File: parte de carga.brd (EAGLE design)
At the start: 74.6 x 102.9 mm, 33 parts, among them IC1 MCP73831T-2ACI_OT, IC10 741G3157DBVR, IC15 LMV321AIDCKR, IC16 LMV321AIDCKR, IC2 ESP32-S3-WROOM-1-N16R8, IC5 LMV321AIDCKR, IC7 AD8226ARZ, IC9 LP38692MP-3.3_NOPB, J1 USB3500-30-A-KIT

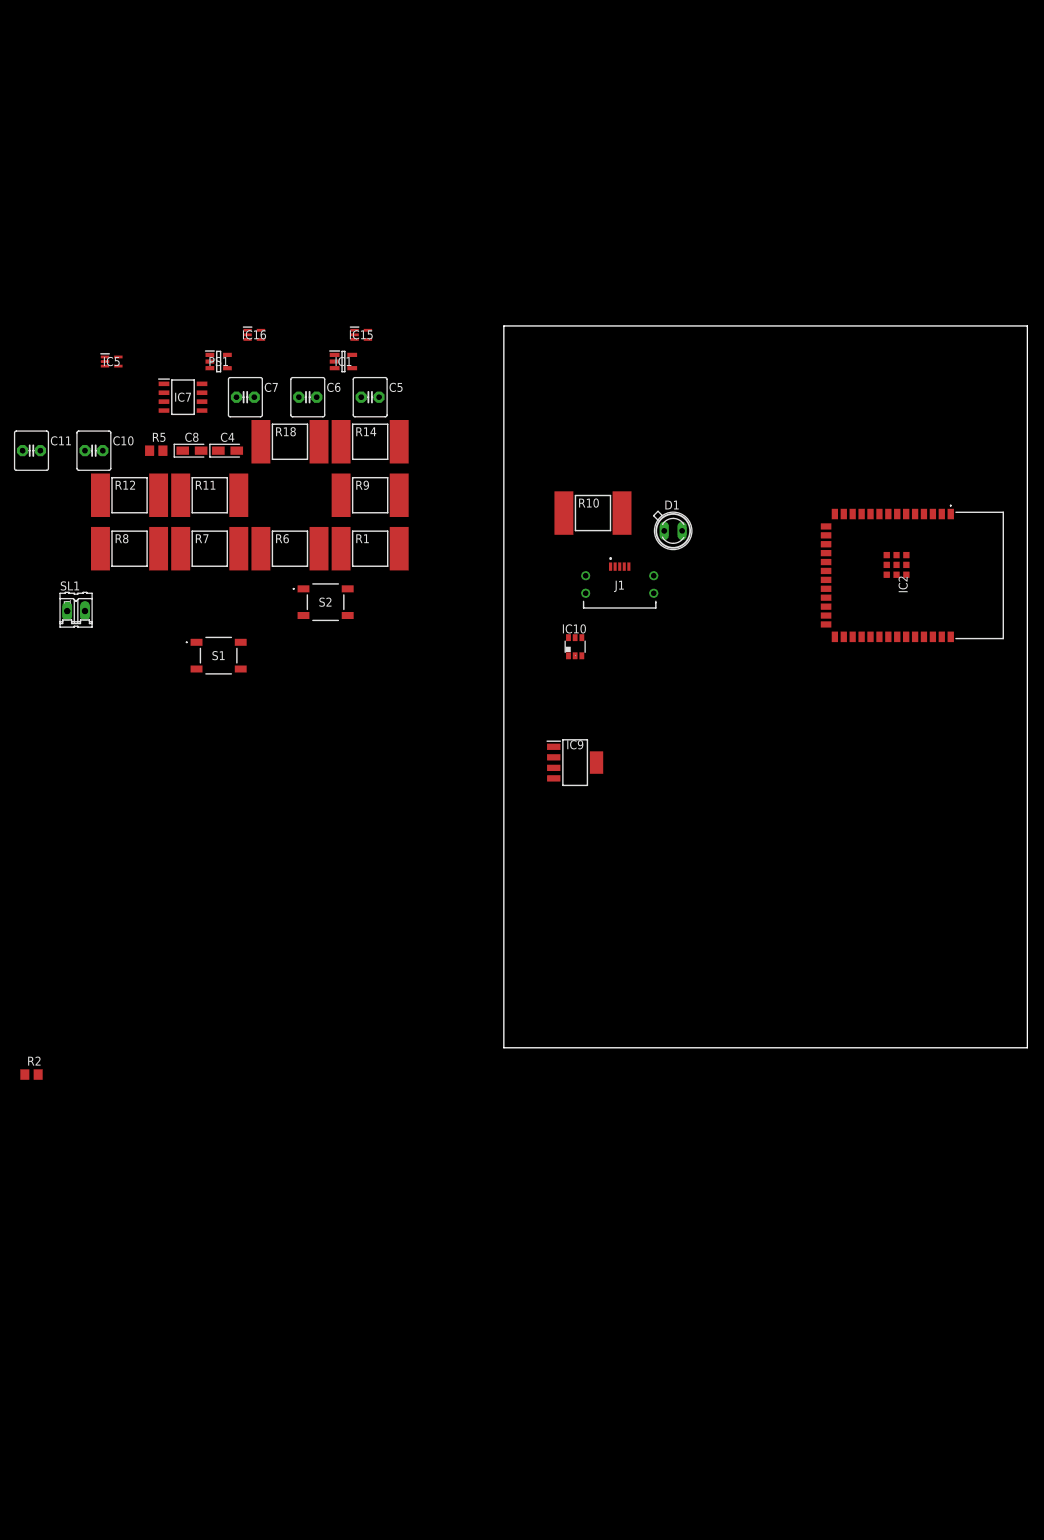
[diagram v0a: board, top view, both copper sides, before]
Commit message: arregle las resistencias, condensadores y diodo
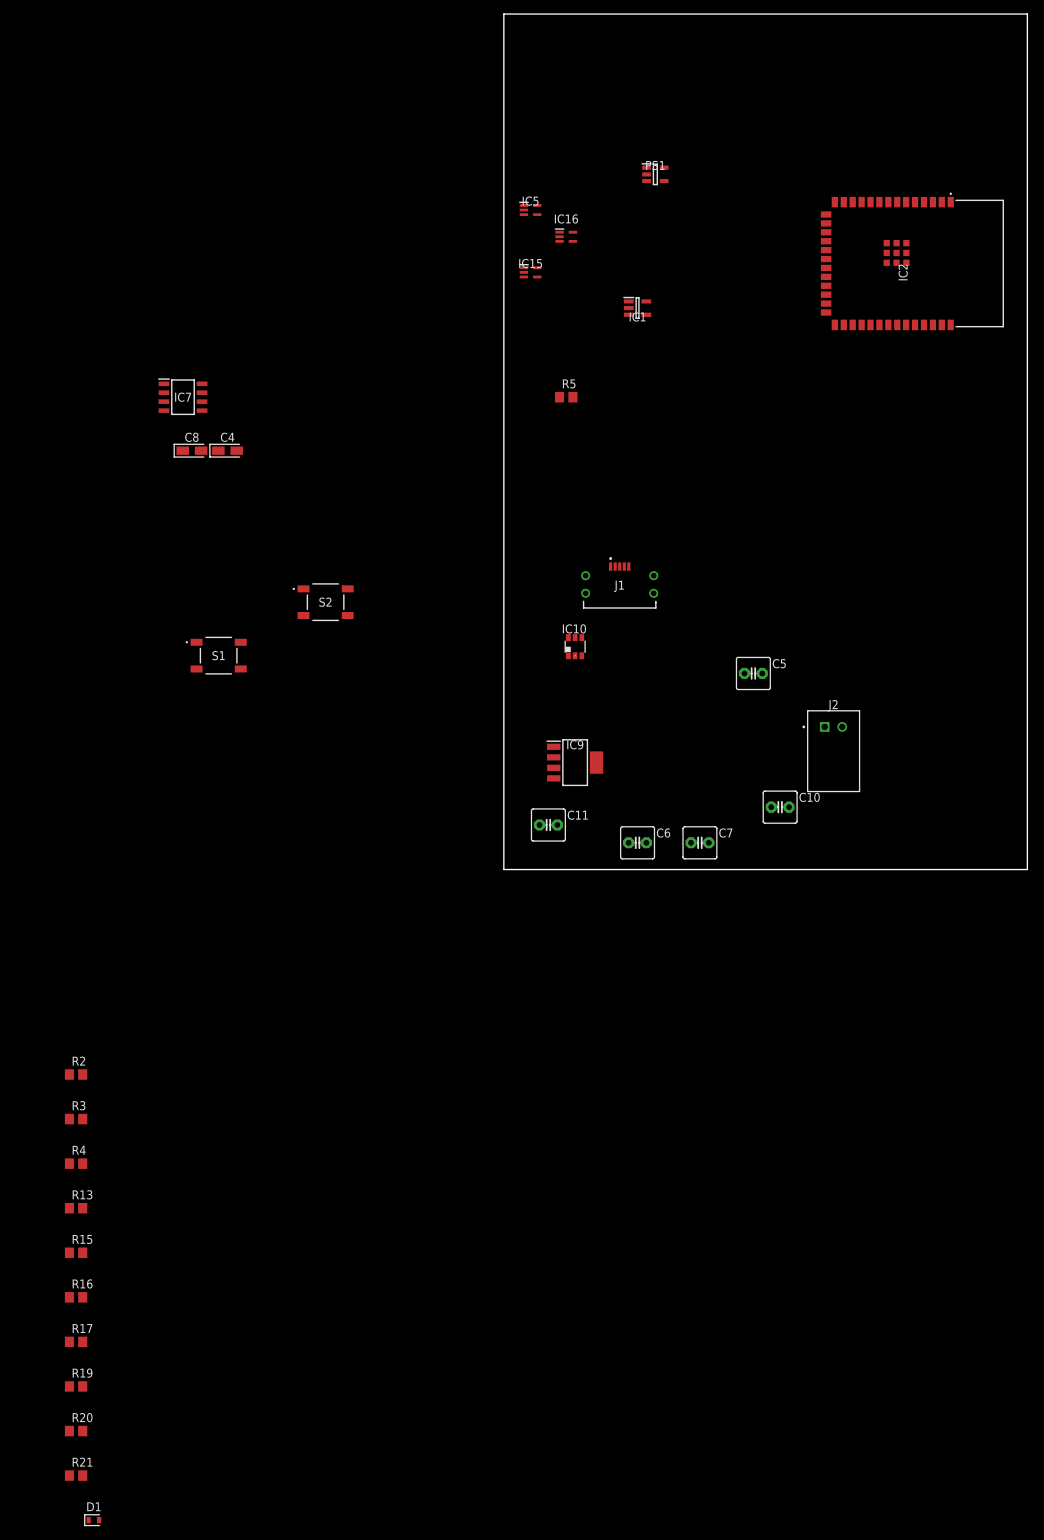
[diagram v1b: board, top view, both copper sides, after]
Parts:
- removed R1: 2k, resistor-shunt:BVS
- removed R10: 220, resistor-shunt:BVS
- removed R11, R12, R8: 10k, resistor-shunt:BVS
- removed R14: 1.6k, resistor-shunt:BVS
- removed R18, R9: 450, resistor-shunt:BVS
- removed R6: 3.2k, resistor-shunt:BVS
- removed R7: 1k, resistor-shunt:BVS
- removed SL1: (no value), con-amp-quick:02P
- added J2: S2B-XH-A, Connector:S2B-XH-A
- added R13: 1.6k, rcl:R0805
- added R15, R21, R4: 10k, rcl:R0805
- added R16: 3.2k, rcl:R0805
- added R17: 1k, rcl:R0805
- added R19, R20: 450, rcl:R0805
- added R3: 2k, rcl:R0805
- C10, C11, C5, C6, C7: device capacitor-wima:C2.5-6 -> capacitor-wima:C2.5-5
- D1: value SFH482 -> CHIP-FLAT-G_0603-0.35MM; device led:SFH482 -> LED:LEDC1608X35N_FLAT-G
- R2: value (none) -> 220
- moved D1 163.4 mm to (-58.4, -90.2)
- moved C10 110.2 mm to (39.4, 11.4)
- moved C11 90.9 mm to (6.35, 8.89)
- moved C7 90.7 mm to (27.9, 6.35)
- moved C6 79.0 mm to (19.1, 6.35)
- moved PS1 67.7 mm to (21.6, 101.6)
- moved C5 67.3 mm to (35.6, 30.5)
- moved IC5 63.5 mm to (3.81, 96.5)
- moved R5 58.9 mm to (8.89, 69.8)
- moved IC16 46.6 mm to (8.89, 92.7)
- moved IC2 44.5 mm to (58.4, 88.9)
- moved IC1 42.6 mm to (19.1, 82.5)
- moved IC15 25.7 mm to (3.81, 87.6)
- moved R2 6.35 mm to (-61.0, -26.7)
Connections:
- removed net N$7: C7.1, IC5.4, R9.1
- new net N$14: C5.2, R13.1
- net +5V: now also R21.2, R4.2; no longer R11.1, R12.1
- net +BATT: now also J2.1; no longer SL1.2
- net GND: now also J2.2, R3.1; no longer R1.2, SL1.1
- net N$1: now also D1.C, R2.2; no longer D1.K, R10.1
- net N$13: now also R17.2; no longer R7.1
- net N$2: now also R2.1; no longer R10.2
- net N$3: now also R3.2; no longer R1.1
- net N$4: now also R4.1; no longer R11.2
- net N$46: now also R13.2, R16.1; no longer R14.1, R6.2
- net N$47: now also R15.1, R16.2; no longer R6.1, R8.2
- net N$5: now also R21.1; no longer R12.2
- net N$6: now also IC16.3, IC16.4, R15.2, R19.1; no longer C5.2, R14.2
- net N$8: now also C7.1, IC5.4, R20.2; no longer IC16.3, IC16.4, R18.2, R8.1
- net N$9: now also R19.2, R20.1; no longer R18.1, R9.2
- net VSS: now also R17.1; no longer R7.2
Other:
- board size 74.6 x 102.9 mm -> 74.6 x 121.9 mm

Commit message: ya agregue las capas de gnd falta que arreglen los componentes
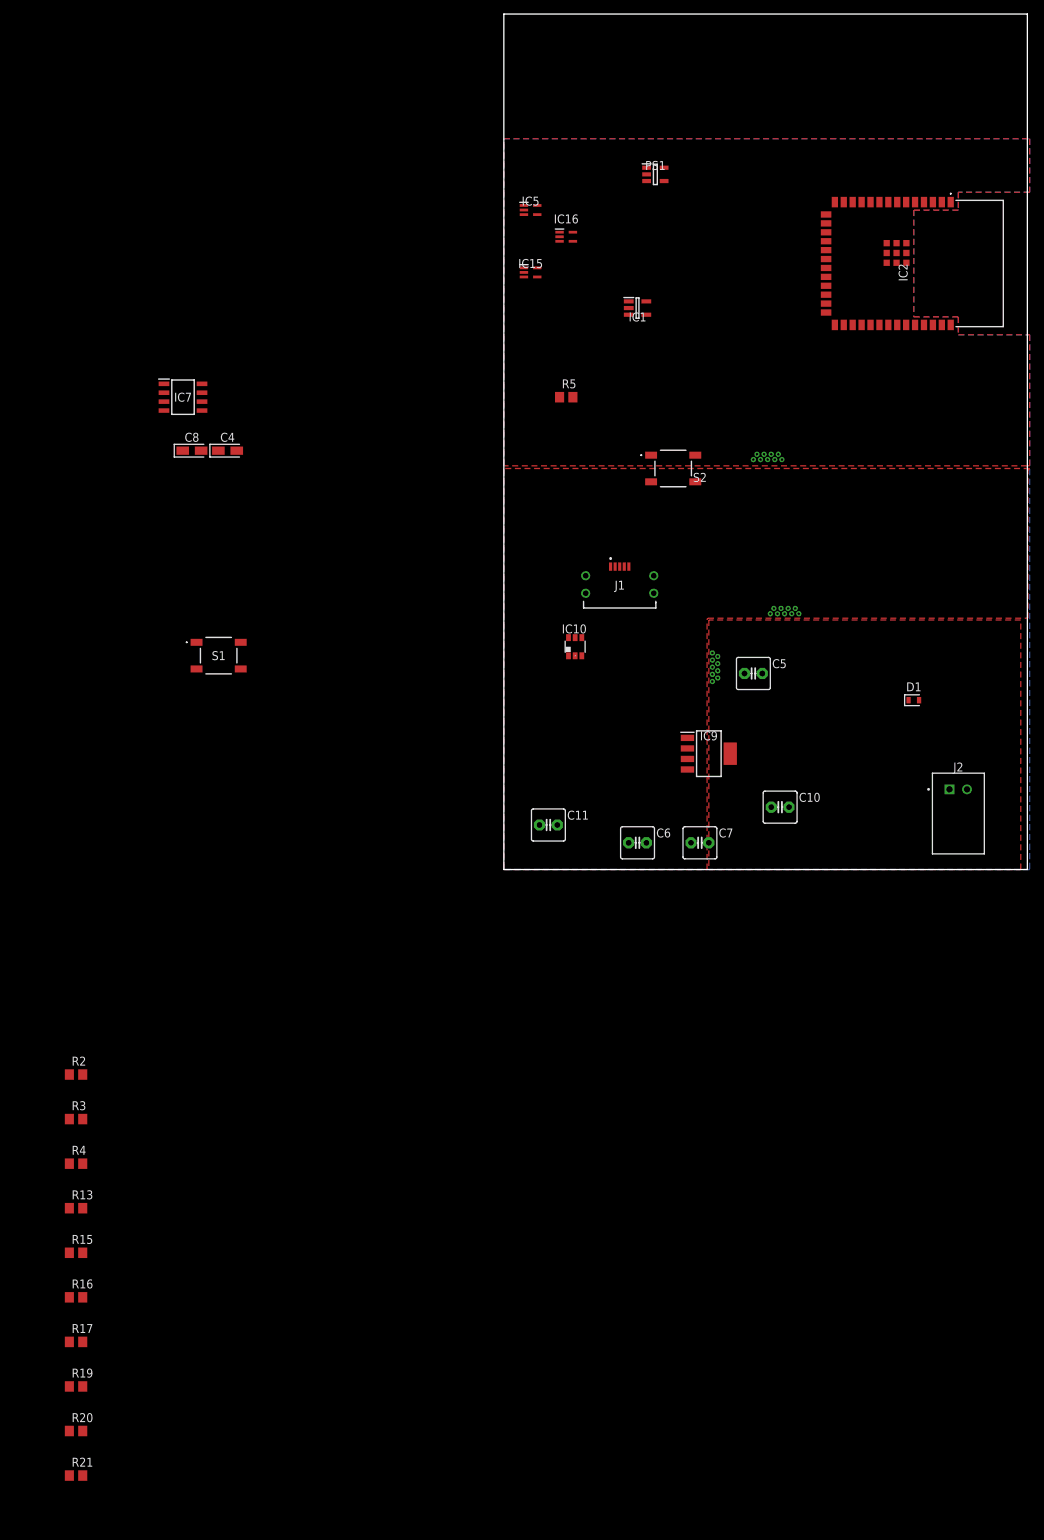
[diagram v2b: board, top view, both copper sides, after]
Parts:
- moved D1 165.2 mm to (58.4, 26.7)
- moved S2 53.1 mm to (24.1, 59.7)
- moved J2 19.9 mm to (63.5, 14.0)
- moved IC9 19.1 mm to (29.2, 19.1)
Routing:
- added copper zone on layer 1, net GND
- added copper zone on layer 16, net GND

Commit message: acomode componentes en la board Harold Astudillo
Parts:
- moved R19 185.7 mm to (21.6, 95.2)
- moved R15 162.1 mm to (19.1, 88.9)
- moved R16 140.3 mm to (33.0, 45.7)
- moved R13 135.7 mm to (30.5, 54.6)
- moved R20 129.5 mm to (25.4, 19.1)
- moved R17 127.0 mm to (21.6, 31.8)
- moved R21 117.4 mm to (12.7, 7.62)
- moved R4 94.8 mm to (16.5, 15.2)
- moved R3 86.3 mm to (11.4, 14.0)
- moved R2 81.0 mm to (7.62, 16.5)
- moved IC7 77.7 mm to (31.8, 76.2)
- moved C8 63.8 mm to (19.1, 68.6), turned to 180 degrees
- moved C4 52.5 mm to (12.7, 68.6)
- moved S1 51.4 mm to (10.2, 25.4)
- moved J1 47.6 mm to (49.5, 7.62)
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
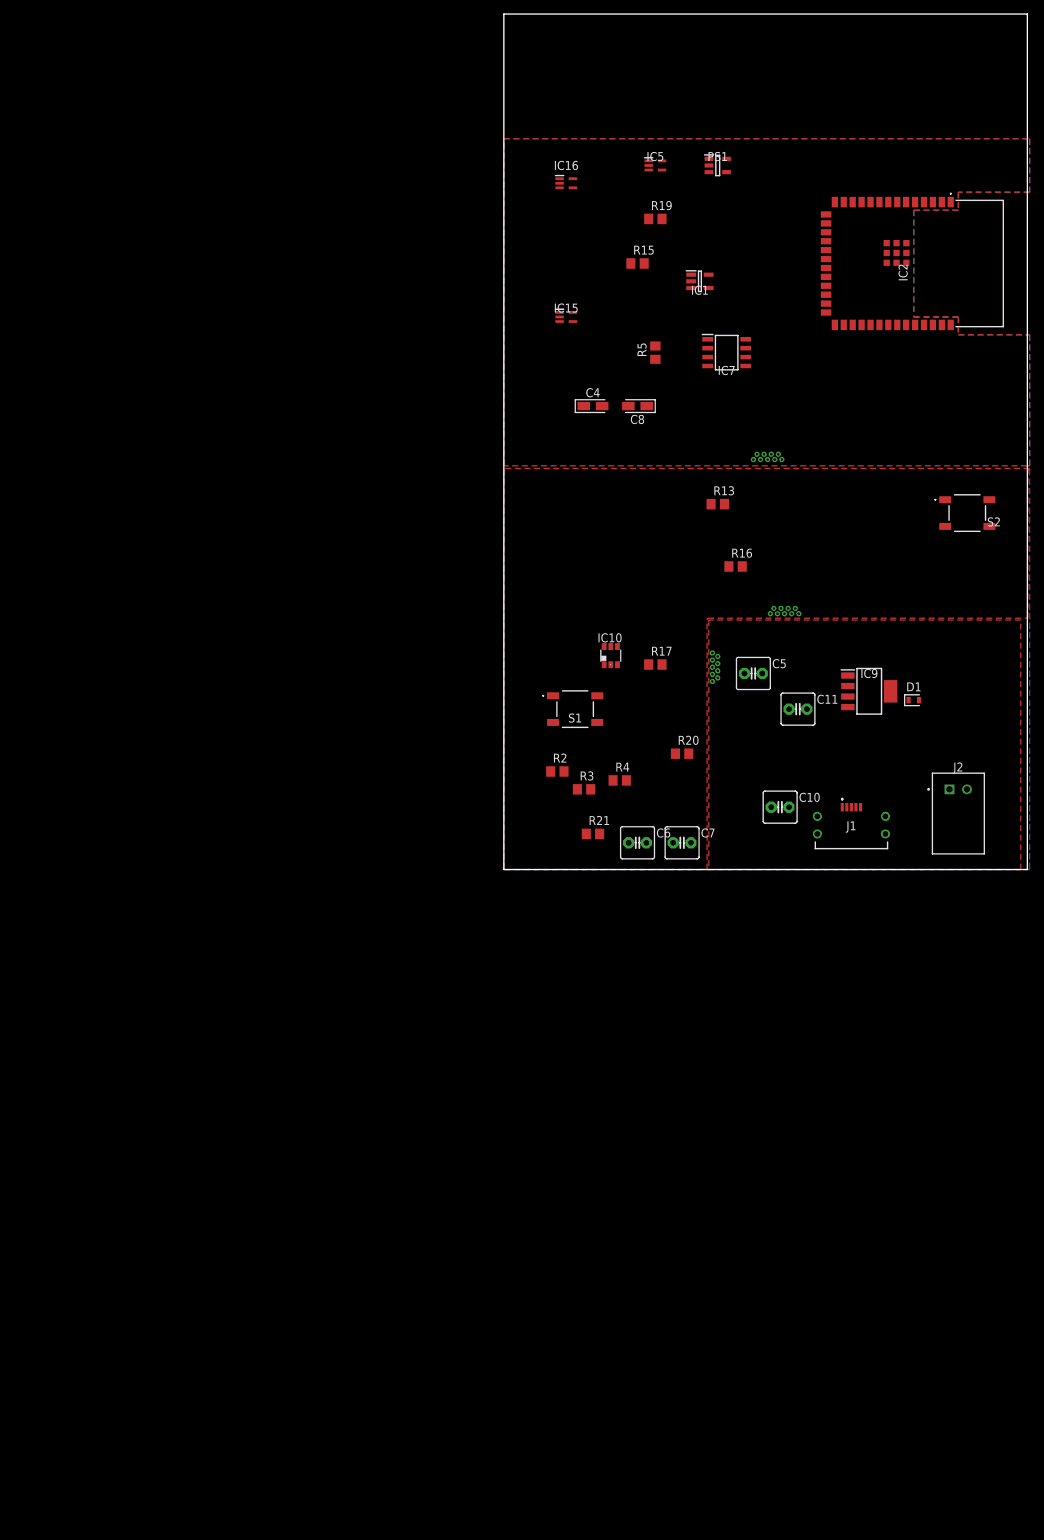
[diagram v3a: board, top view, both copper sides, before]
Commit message: areglé parte del puerto usb, y el conector de elctrodos, saqué un conector de 3 pines rx. tx, gnd. saqué un conector para el display
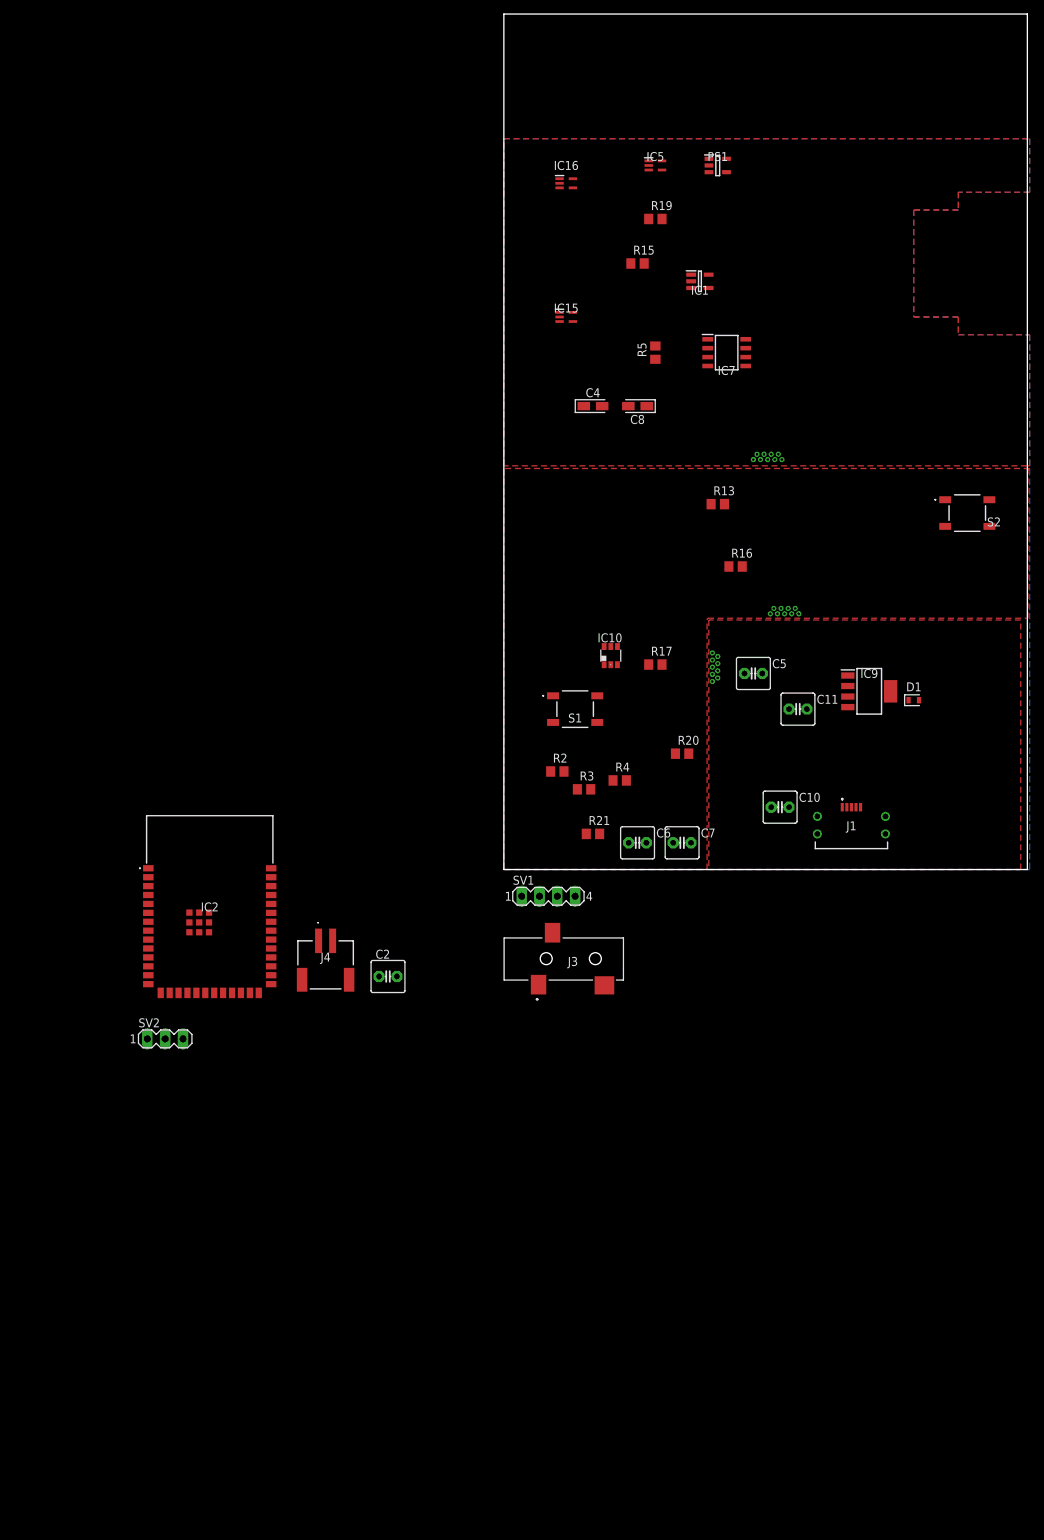
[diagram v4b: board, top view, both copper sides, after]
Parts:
- removed J2: S2B-XH-A, Connector:S2B-XH-A
- added C2: 0.1uF, capacitor-wima:C2.5-5
- added J3: SJ-3523-SMT-TR, SJ-3523-SMT-TR:SJ3523SMTTR
- added J4: 1769, 1769:1769
- added SV1: (no value), con-lstb:MA04-1
- added SV2: (no value), con-lstb:MA03-1
- IC2: value ESP32-S3-WROOM-1-N16R8 -> ESP32-S3-WROOM-1-N16R2; device ESP32-S3-WROOM-1-N16R8:ESP32S3WROOM1N16R8 -> ESP32-S3-WROOM-1-N16R2:ESP32S3WROOM1N16R2
- moved IC2 135.7 mm to (-41.9, -2.54), turned to 0 degrees
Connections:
- net N$19 renamed VOUT1
- removed net N$20: IC7.4
- removed net N$30: IC2.14
- new net +D: IC2.14, J1.3
- new net -D: IC2.13, J1.2
- new net N$19: C8.1, J4.1
- net +3V3: now also C2.1, SV1.2
- net +BATT: no longer C8.1, J2.1
- net GND: now also C2.2, J4.2, SV1.1, SV2.1; no longer J1.4, J2.2
- net N$11: now also IC7.1, J3.3; no longer IC2.13
- net N$17: now also IC7.4, J3.2; no longer IC7.1
- net RX: now also SV2.3
- net SCL: now also SV1.3
- net SDA: now also SV1.4
- net TX: now also SV2.2
- net VSS: now also J3.1
